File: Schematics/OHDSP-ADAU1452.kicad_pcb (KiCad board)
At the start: 4 copper layers, 100 x 100 mm, 304 parts, among them CN201 COAX, CN401 COAX, CN402 COAX, CN405 COAX, CN406 COAX, P201 CONN_2x1, P203 CONN_6X2, P204 CONN_6x1, P301 CONN_2x1, P302 CONN_2x1, P303 PIN, P304 PIN, P305 PIN, P306 PIN, P601 CONN_02X05, P602 CONN_02X05, P603 CONN_02X05, P604 CONN_02X05, P605 CONN_3x1, P606 CONN_6X2, P607 CONN_02X05, P608 CONN_02X05, P609 CONN_02X20, P610 CONN_02X05, P611 CONN_5x1, P613 CONN_02X05, P614 CONN_02X05, P615 CONN_02X05, P616 CONN_02X05, SW202 SWITCH, U201 ADAU1452WBCPZ, U202 ADM13307-5ARZ, U203 25AA1024, U301 IC-REG-XRP7659ISTR-F, U302 IC-REG-XRP7659ISTR-F, U304 IC-REG-XC6210B332MR, U305 IC-REG-XC6210B332MR, U401 NB3L553, U501 IC-SPDIF-RX-OPTO, U502 IC-SPDIF-TX-OPTO, X201 24M576

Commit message: PCB Work, minor schematic changes
Removed cap and LED, changed one net label
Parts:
- removed C405: 100n, OHDSP-Footprints-Pretty:SMD-0805
- removed D305, D307: LED, OHDSP-Footprints-Pretty:SMD-1206
- removed R309, R311: 470R, OHDSP-Footprints-Pretty:SMD-0805
- C201, R202, R203: moved to B.Cu
- moved R674 576.5 mm to (307.2, 80.4), turned to 90 degrees
- moved R645 519.3 mm to (256.3, 57.0)
- moved R628 494.3 mm to (198.4, 68.3)
- moved C605 465.2 mm to (119.0, 175.6)
- moved D606 458.7 mm to (50.8, 183.1)
- moved D611 458.7 mm to (34.3, 203.5)
- moved C601 458.7 mm to (134.6, 162.8)
- moved C602 458.7 mm to (134.6, 166.6)
- moved C603 458.7 mm to (134.6, 170.4)
- moved C604 458.7 mm to (134.6, 174.2)
- moved C607 458.7 mm to (134.6, 178.1)
- moved C608 458.7 mm to (134.6, 181.9)
- moved D601 458.7 mm to (52.1, 203.5)
- moved D602 458.7 mm to (53.3, 208.5)
- moved D603 458.7 mm to (53.3, 212.3)
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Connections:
- R205 pad 1: /ADAU1452/SS_M/MP0 -> /ADAU1452/M_SS
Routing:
- net Net-(C403-Pad1): track 14.5 -> 16.4 mm
- net Net-(R404-Pad1): track 0.00 -> 1.49 mm

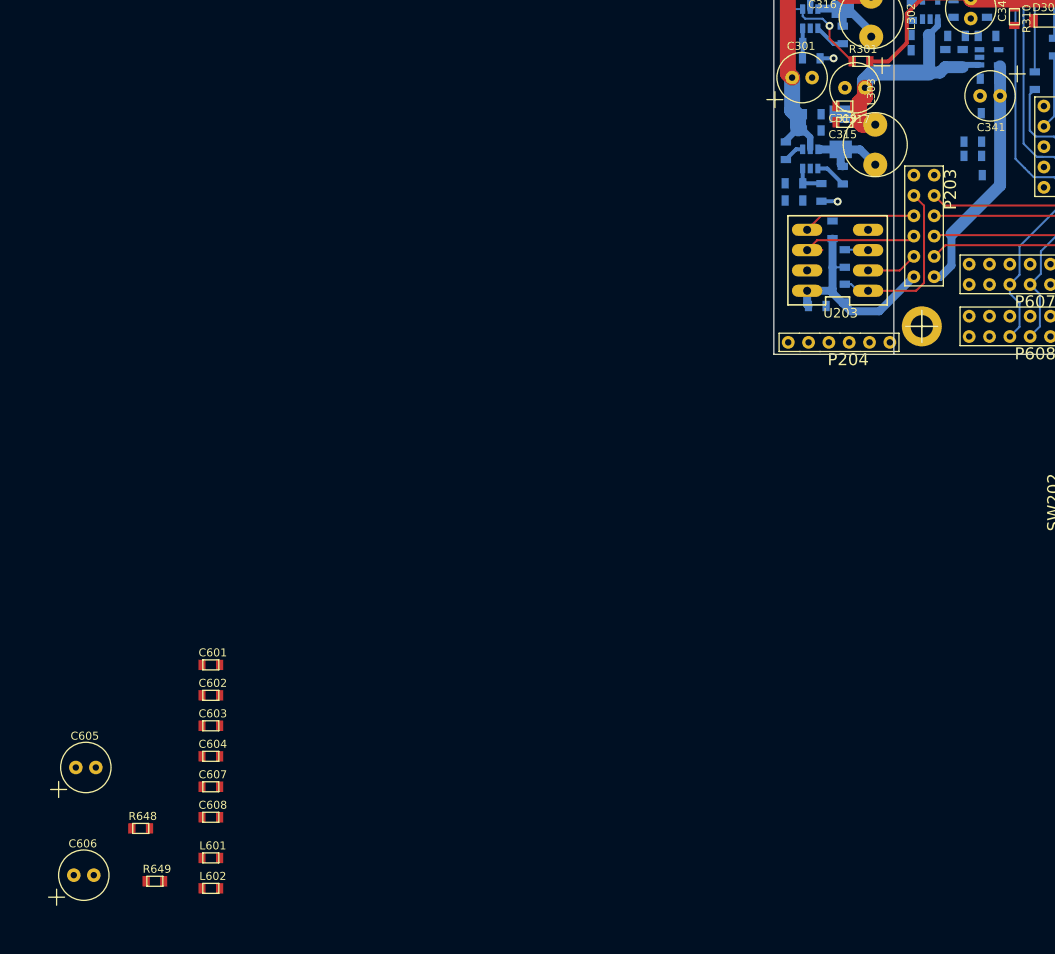
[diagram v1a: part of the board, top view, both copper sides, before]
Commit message: PCB work, remove 5v from I2C headers
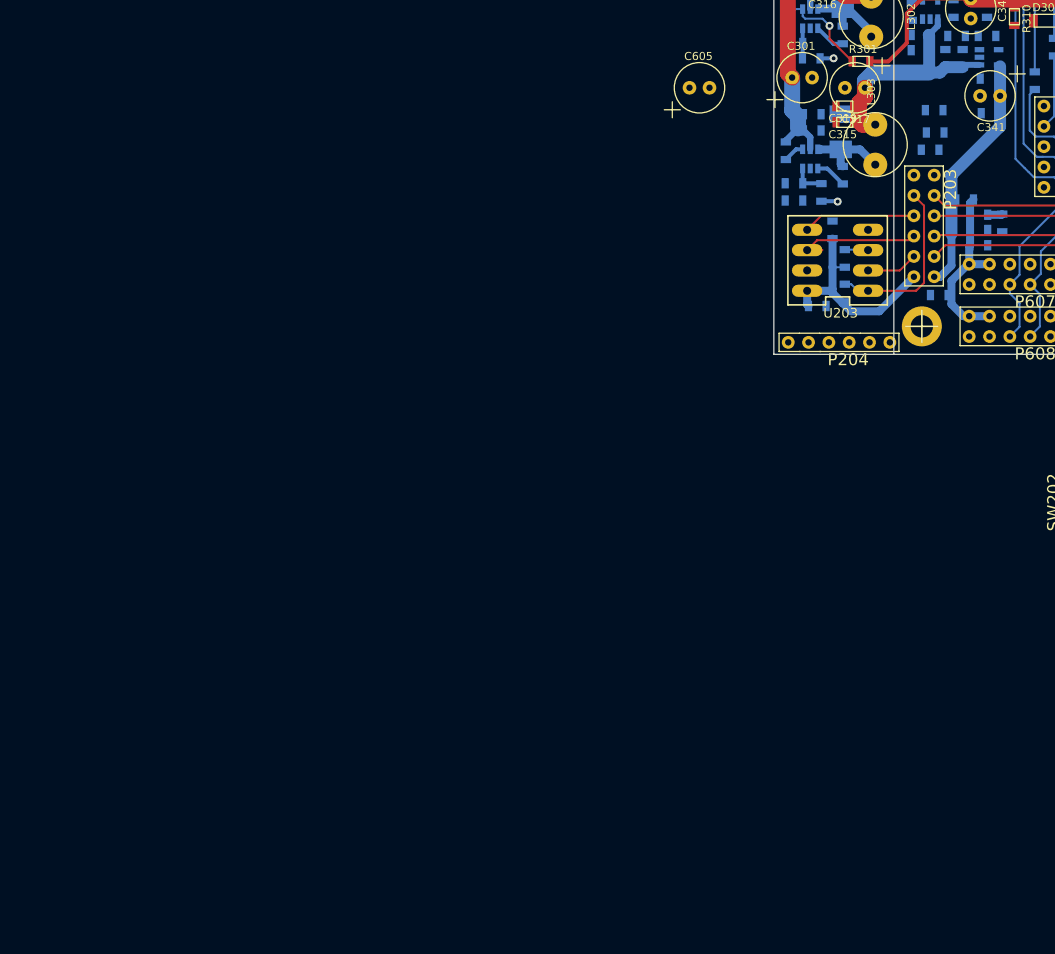
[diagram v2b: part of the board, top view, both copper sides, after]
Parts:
- removed C602: 100n, OHDSP-Footprints-Pretty:SMD-0805
- removed C604: 22u, OHDSP-Footprints-Pretty:SMD-0805
- removed C606: 220u, OHDSP-Footprints-Pretty:CAP-TH-D6.3mmP2.5mm
- removed C608: 100p, OHDSP-Footprints-Pretty:SMD-0805
- removed L602: 600R@100MHz, OHDSP-Footprints-Pretty:SMD-0805
- removed R649: 47R, OHDSP-Footprints-Pretty:SMD-0805
- added C609: 100n, OHDSP-Footprints-Pretty:SMD-0805, B.Cu at (225.7, 116.6)
- C601, C603, C607, L601, R648: moved to B.Cu
- moved R648 129.9 mm to (230.6, 106.6), turned to 180 degrees
- moved L601 125.1 mm to (228.9, 104.6)
- moved C607 121.5 mm to (233.6, 107.6), turned to 270 degrees
- moved C605 114.5 mm to (195.7, 90.7)
- moved C603 114.3 mm to (230.6, 108.5)
- moved C601 109.4 mm to (230.6, 110.4)
- moved C201 8.79 mm to (225.2, 96.3)
- moved R202 7.48 mm to (225.0, 93.5)
- moved R203 5.43 mm to (224.5, 98.4)
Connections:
- P607 pad 4: GNDD -> Net-(C601-Pad1)
- P607 pad 6: Net-(C602-Pad1) -> GNDD
- P608 pad 4: GNDD -> Net-(C601-Pad1)
- P608 pad 6: Net-(C602-Pad1) -> GNDD
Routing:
- net Net-(C601-Pad1): track 0.00 -> 22.2 mm
- net Net-(C607-Pad1): track 0.00 -> 1.86 mm

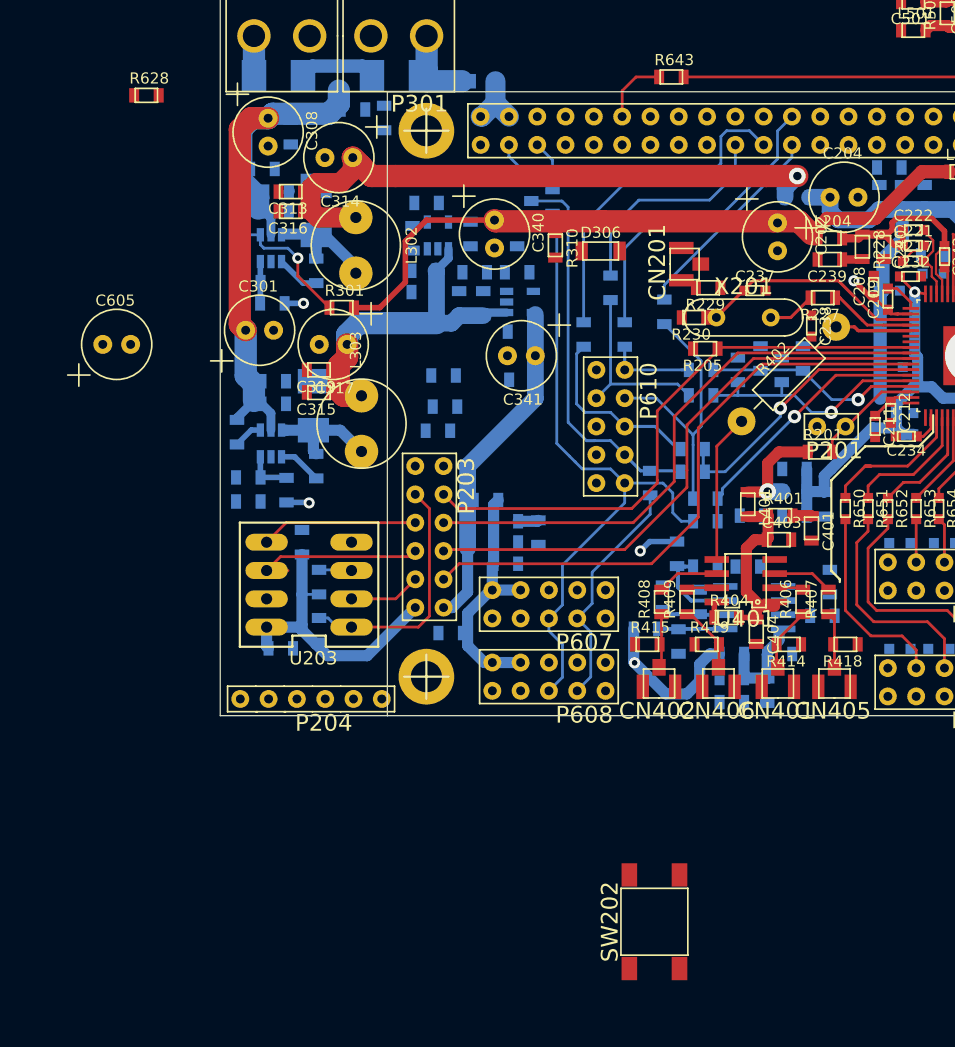
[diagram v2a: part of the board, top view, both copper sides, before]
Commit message: PCB work, added manual reset to Pi header
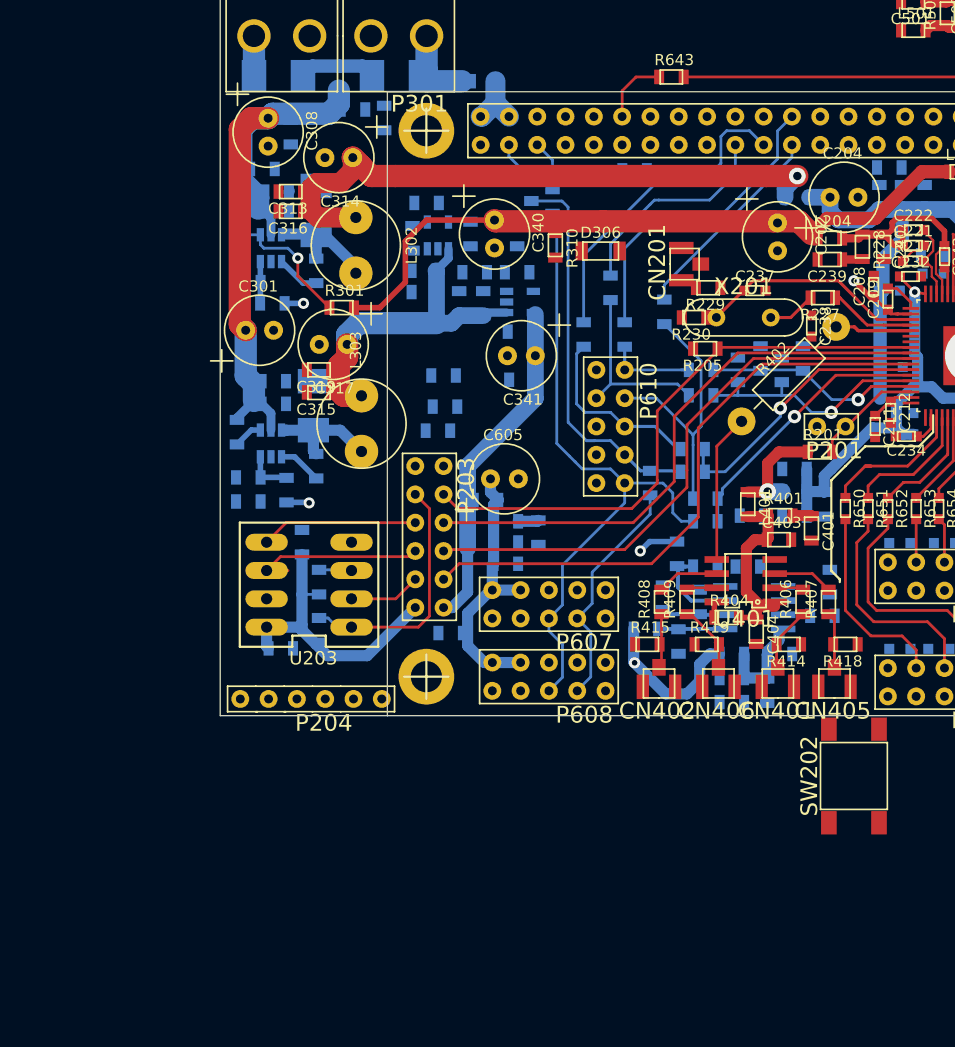
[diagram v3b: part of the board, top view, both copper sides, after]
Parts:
- R628: value 0R -> 1k; moved to B.Cu
- moved R628 44.3 mm to (242.2, 75.1)
- moved C605 36.8 mm to (230.5, 102.7)
- moved SW202 22.2 mm to (261.9, 129.4)
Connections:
- C231 pad 1: Net-(C231-Pad1) -> /ADAU1452/MRST
- R233 pad 2: Net-(C231-Pad1) -> /ADAU1452/MRST
- R628 pad 1: /Connectors/PI_3V3 -> /ADAU1452/MRST
- R628 pad 2: Net-(P609-Pad1) -> Net-(P609-Pad13)
- SW202 pad 1: Net-(C231-Pad1) -> /ADAU1452/MRST
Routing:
- net Net-(C601-Pad1): track 22.2 -> 24.4 mm
- net Net-(P609-Pad21): track 30.4 -> 28.7 mm
- net Net-(P609-Pad19): track 20.1 -> 19.3 mm

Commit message: PCB work
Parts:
- C241, C250: moved to F.Cu
- R643, R674: moved to B.Cu
- moved SW202 72.5 mm to (235.3, 62.0), turned to 90 degrees
- moved R674 32.4 mm to (282.7, 101.6), turned to 0 degrees
- moved C241 23.7 mm to (309.9, 81.7)
- moved C250 18.3 mm to (307.3, 81.7)
- moved R601 15.5 mm to (287.1, 84.2), turned to 270 degrees
- moved R602 11.6 mm to (285.9, 74.5), turned to 270 degrees
- moved R603 6.67 mm to (284.2, 78.2), turned to 270 degrees
- moved R643 2.36 mm to (243.6, 68.1)
- moved R647 1.89 mm to (279.9, 75.2), turned to 0 degrees
- moved R634 0.97 mm to (273.1, 76.2)
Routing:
- net /ADAU1452/MRST: track 0.00 -> 72.1 mm, vias 0 -> 3
- net /Connectors/RPI_LRCLK: track 0.00 -> 16.5 mm
- net /Connectors/RPI_BCLK: track 39.4 -> 48.9 mm
- net Net-(P609-Pad40): track 0.00 -> 5.86 mm
- net Net-(P609-Pad38): track 0.00 -> 5.47 mm
- net /Connectors/RPI_SDATA_OUT: track 0.00 -> 4.02 mm
- net /ADAU1452/ADCIN_SDATA0: track 24.6 -> 20.6 mm
- net /ADAU1452/ADCIN_BCLK3: track 30.4 -> 34.2 mm, vias 0 -> 1
- net Net-(P609-Pad12): track 6.15 -> 2.74 mm
- net VAA: track 61.7 -> 64.7 mm
- net Net-(P609-Pad35): track 0.03 -> 2.99 mm
- net Net-(P609-Pad13): track 0.00 -> 2.42 mm
- net /ADAU1452/ADCIN_BCLK0: track 29.2 -> 27.5 mm
- net /ADAU1452/ADCIN_LRCLK3: track 34.4 -> 36.1 mm, vias 0 -> 1
- net /ADAU1452/ADCIN_LRCLK0: track 33.7 -> 32.1 mm
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- added copper zone on B.Cu, net GNDD
- added copper zone on In1.Cu, net GNDD

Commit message: PCB work
Also playing with via sizes...
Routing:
- net /ADAU1452/DACOUT_LRCLK0: track 13.9 -> 12.2 mm
- net /ADAU1452/DACOUT_SDATA0: track 10.3 -> 11.2 mm
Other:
- rule via_min_size: 0.6 -> 0.5
